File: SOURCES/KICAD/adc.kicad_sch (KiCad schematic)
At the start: 224 parts

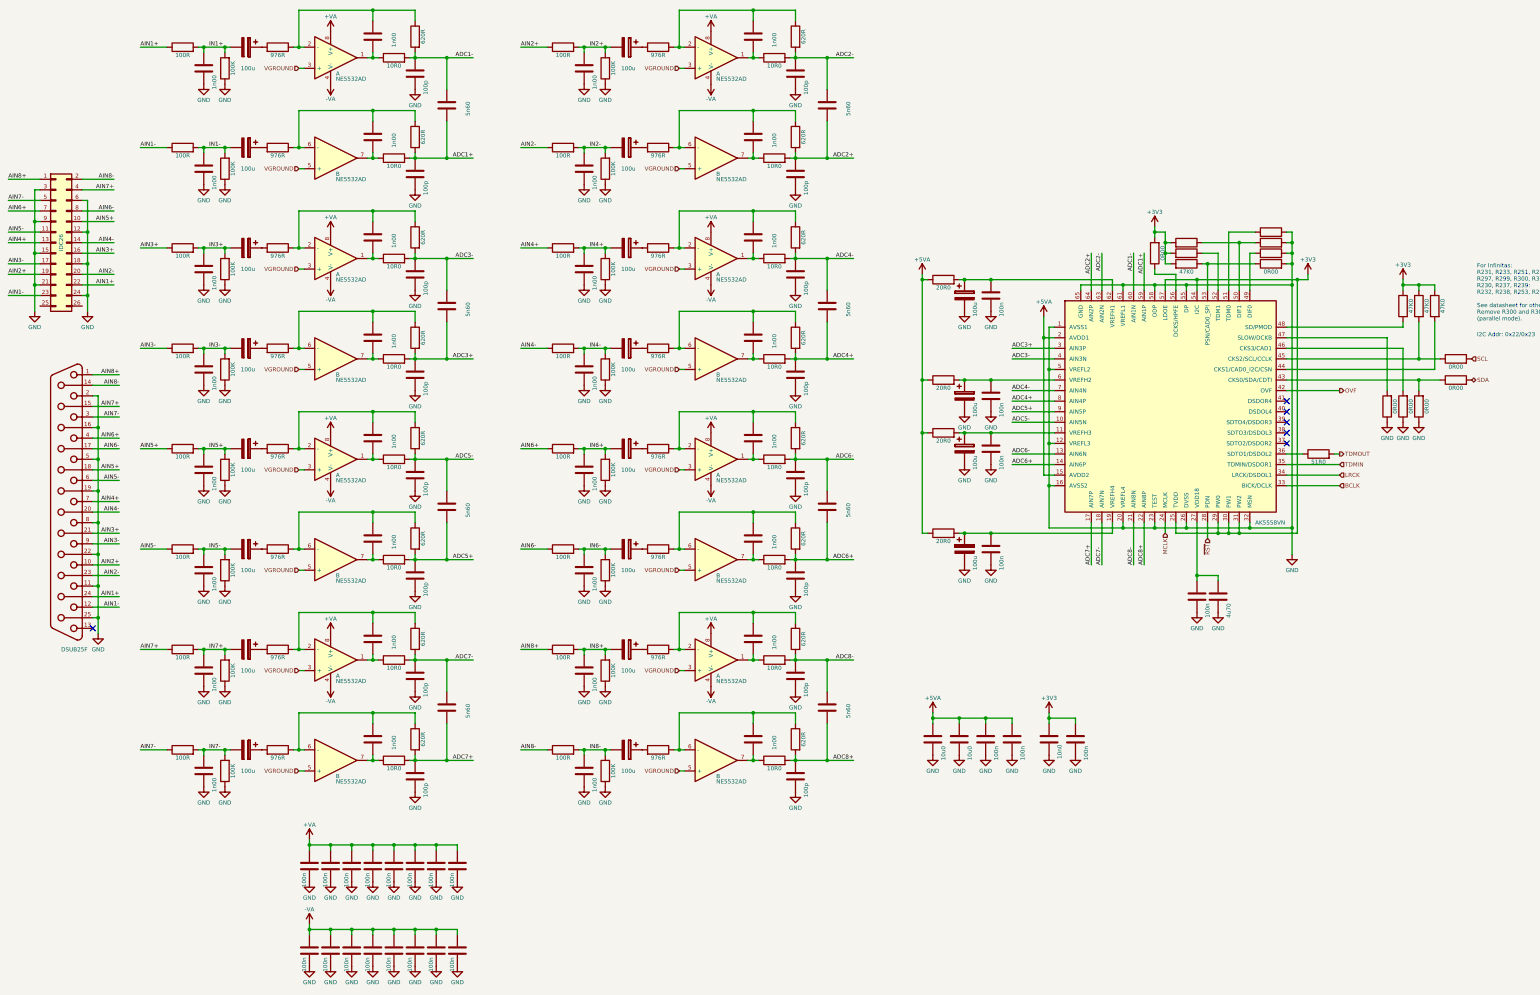
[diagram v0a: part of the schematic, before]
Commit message: Rescue footprints to local library
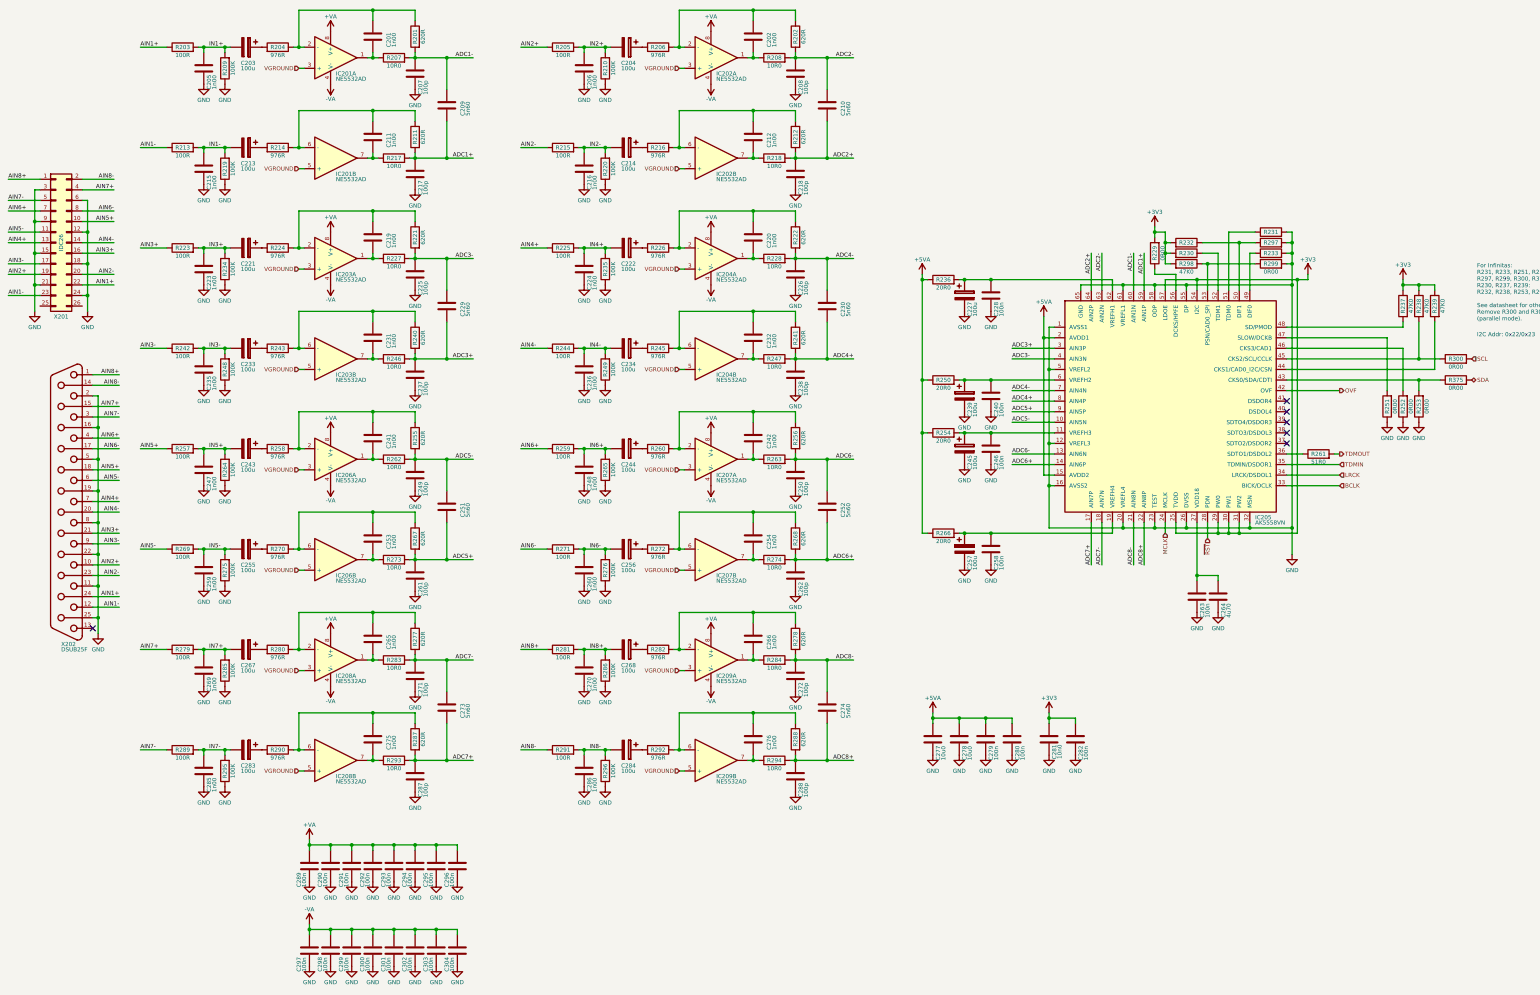
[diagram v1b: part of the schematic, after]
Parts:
- C201, C202, C205, C206, C207, C208, C209, C210, C211, C212, C215, C216, C217, C218, C219, C220, C223, C224, C225, C226, C228, C229, C230, C231, C232, C235, C236, C237, C238, C240, C241, C242, C246, C247, C248, C249, C250, C251, C252, C253, C254, C258, C259, C260, C261, C262, C263, C264, C265, C266, C269, C270, C271, C272, C273, C274, C275, C276, C277, C278, C279, C280, C281, C282, C285, C286, C287, C288, C289, C290, C291, C292, C293, C294, C295, C296, C297, C298, C299, C300, C301, C302, C303, C304: renamed from ?; footprint rklib:C0805-X7R -> AnalogIO-x8:C0805-X7R
- C203, C204, C213, C214, C221, C222, C227, C233, C234, C239, C243, C244, C245, C255, C256, C257, C267, C268, C283, C284: renamed from ?; footprint Capacitors_ThroughHole:C_Radial_D5_L11_P2 -> AnalogIO-x8:RD2_D5_L11
- X201: renamed from ?; footprint Connect:IDC_Header_Straight_26pins -> AnalogIO-x8:IDC26
- X202: renamed from ?; footprint rklib:DSUB25FC -> AnalogIO-x8:DSUB25FC
- gave numbers to parts that had none: 110
